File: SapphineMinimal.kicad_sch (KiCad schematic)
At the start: 0 parts

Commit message: daily update
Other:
- note added: "Optional Winc1500 WiFi module add on"
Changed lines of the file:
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@@
+    (stroke (width 0) (type default) (color 0 0 0 0))
+  )
+  (polyline (pts (xy 165.1 123.19) (xy 165.1 168.91))
     (stroke (width 0) (type default) (color 0 0 0 0))
   )
@@
     (stroke (width 0) (type default) (color 0 0 0 0))
   )
+  (polyline (pts (xy 255.27 123.19) (xy 255.27 168.91))
+    (stroke (width 0) (type default) (color 0 0 0 0))
+  )
   (wire (pts (xy 30.48 20.32) (xy 29.21 21.59))
     (stroke (width 0) (type default) (color 0 0 0 0))
@@
     (stroke (width 0) (type default) (color 0 0 0 0))
   )
+  (polyline (pts (xy 255.27 168.91) (xy 165.1 168.91))
+    (stroke (width 0) (type default) (color 0 0 0 0))
+  )
   (wire (pts (xy 162.56 110.49) (xy 203.2 110.49))
     (stroke (width 0) (type default) (color 0 0 0 0))
@@
     (stroke (width 0) (type default) (color 0 0 0 0))
   )
+  (polyline (pts (xy 166.37 123.19) (xy 255.27 123.19))
+    (stroke (width 0) (type default) (color 0 0 0 0))
+  )
   (wire (pts (xy 67.31 68.58) (xy 111.76 68.58))
     (stroke (width 0) (type default) (color 0 0 0 0))
@@
   (wire (pts (xy 48.26 90.17) (xy 111.76 90.17))
     (stroke (width 0) (type default) (color 0 0 0 0))
+  )
+  (text "Optional Winc1500 WiFi module add on" (at 172.72 166.37 0)
+    (effects (font (size 1.27 1.27)) (justify left bottom))
   )
   (label "P3V3" (at 21.59 64.77 0)
@@
       (reference "R306") (unit 1) (value "0") (footprint "Resistor_SMD:R_0603_1608Metric")
     )
+    (path "/00000000-0000-0000-0000-00005e3feed8/daf0bd99-befa-4f90-9212-4e1a6269e40c"
+      (reference "R307") (unit 1) (value "47") (footprint "Resistor_SMD:R_0603_1608Metric")
+    )
+    (path "/00000000-0000-0000-0000-00005e3feed8/73b836e8-41a3-4a83-a239-43a97f5d54a3"
+      (reference "R308") (unit 1) (value "47") (footprint "Resistor_SMD:R_0603_1608Metric")
+    )
+    (path "/00000000-0000-0000-0000-00005e3feed8/15b51247-f7d4-4fb2-a281-1d0f0d3ebd69"
+      (reference "R309") (unit 1) (value "47") (footprint "Resistor_SMD:R_0603_1608Metric")
+    )
+    (path "/00000000-0000-0000-0000-00005e3feed8/8bee83c3-4740-451a-ae50-53d5532ca793"
+      (reference "R310") (unit 1) (value "47") (footprint "Resistor_SMD:R_0603_1608Metric")
+    )
     (path "/00000000-0000-0000-0000-00005e3fe93a/00000000-0000-0000-0000-00005e48c1be"
       (reference "R401") (unit 1) (value "47") (footprint "Resistor_SMD:R_0603_1608Metric")
@@
       (reference "R701") (unit 1) (value "0R25") (footprint "Resistor_SMD:R_0603_1608Metric")
     )
+    (path "/00000000-0000-0000-0000-000063a74ef2/6d43920e-21c5-441e-8415-c5dfb7b75379"
+      (reference "R702") (unit 1) (value "47") (footprint "Resistor_SMD:R_0603_1608Metric")
+    )
+    (path "/00000000-0000-0000-0000-000063a74ef2/44066c90-8c1b-4164-acc8-5fad27e22e40"
+      (reference "R703") (unit 1) (value "47") (footprint "Resistor_SMD:R_0603_1608Metric")
+    )
     (path "/00000000-0000-0000-0000-000063357571/00000000-0000-0000-0000-0000634d9925"
       (reference "R801") (unit 1) (value "4K75") (footprint "Resistor_SMD:R_0603_1608Metric")
@@
       (reference "R838") (unit 1) (value "47K5") (footprint "Resistor_SMD:R_0603_1608Metric")
     )
+    (path "/00000000-0000-0000-0000-000063357571/4b0fc5c4-e883-4a22-b9a8-4f7d5505cc14"
+      (reference "R839") (unit 1) (value "47") (footprint "Resistor_SMD:R_0603_1608Metric")
+    )
+    (path "/00000000-0000-0000-0000-000063357571/0ba43dcf-e8ac-4b48-84ad-6973602d256f"
+      (reference "R840") (unit 1) (value "47") (footprint "Resistor_SMD:R_0603_1608Metric")
+    )
+    (path "/00000000-0000-0000-0000-000063357571/0c45c3ff-9887-4163-9704-1098ef8613b4"
+      (reference "R841") (unit 1) (value "47") (footprint "Resistor_SMD:R_0603_1608Metric")
+    )
+    (path "/00000000-0000-0000-0000-000063357571/ef6922cb-e889-42f1-8d57-45ab4f8f15cc"
+      (reference "R842") (unit 1) (value "47") (footprint "Resistor_SMD:R_0603_1608Metric")
+    )
     (path "/00000000-0000-0000-0000-00005e3fe3dd/00000000-0000-0000-0000-000060b7a41f"

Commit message: Checkpoint
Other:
- sheet SapphireMini_GNSS ports: added GNSS_OUTPUT_POWER; removed GNSS_PWR
- sheet SapphireMini_Power ports: added GNSS_OUTPUT_POWER, GNSS_PWR, SD_OUTPUT_POWER, SD_PWR; removed none
- sheet SapphireMini_SD ports: added SD_OUTPUT_POWER; removed SD_PWR
- sheet Sapphire_Proc ports: added P3V3; removed none
- sheet Sapphire_WiFi ports: added P3V3; removed none

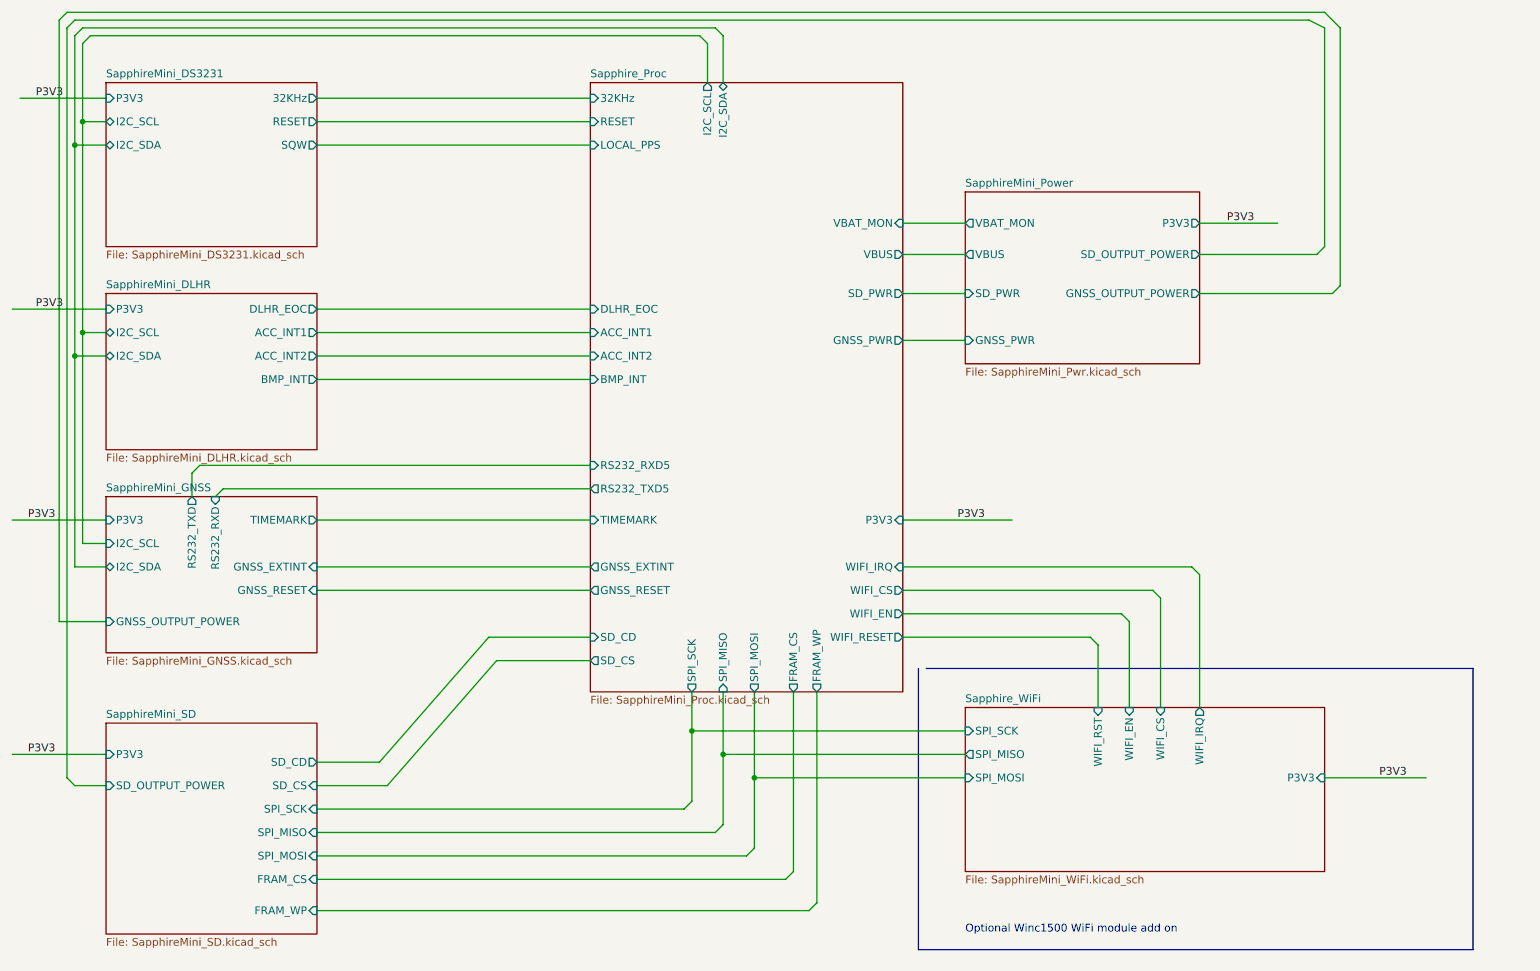
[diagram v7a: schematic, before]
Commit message: Updating for parts avail
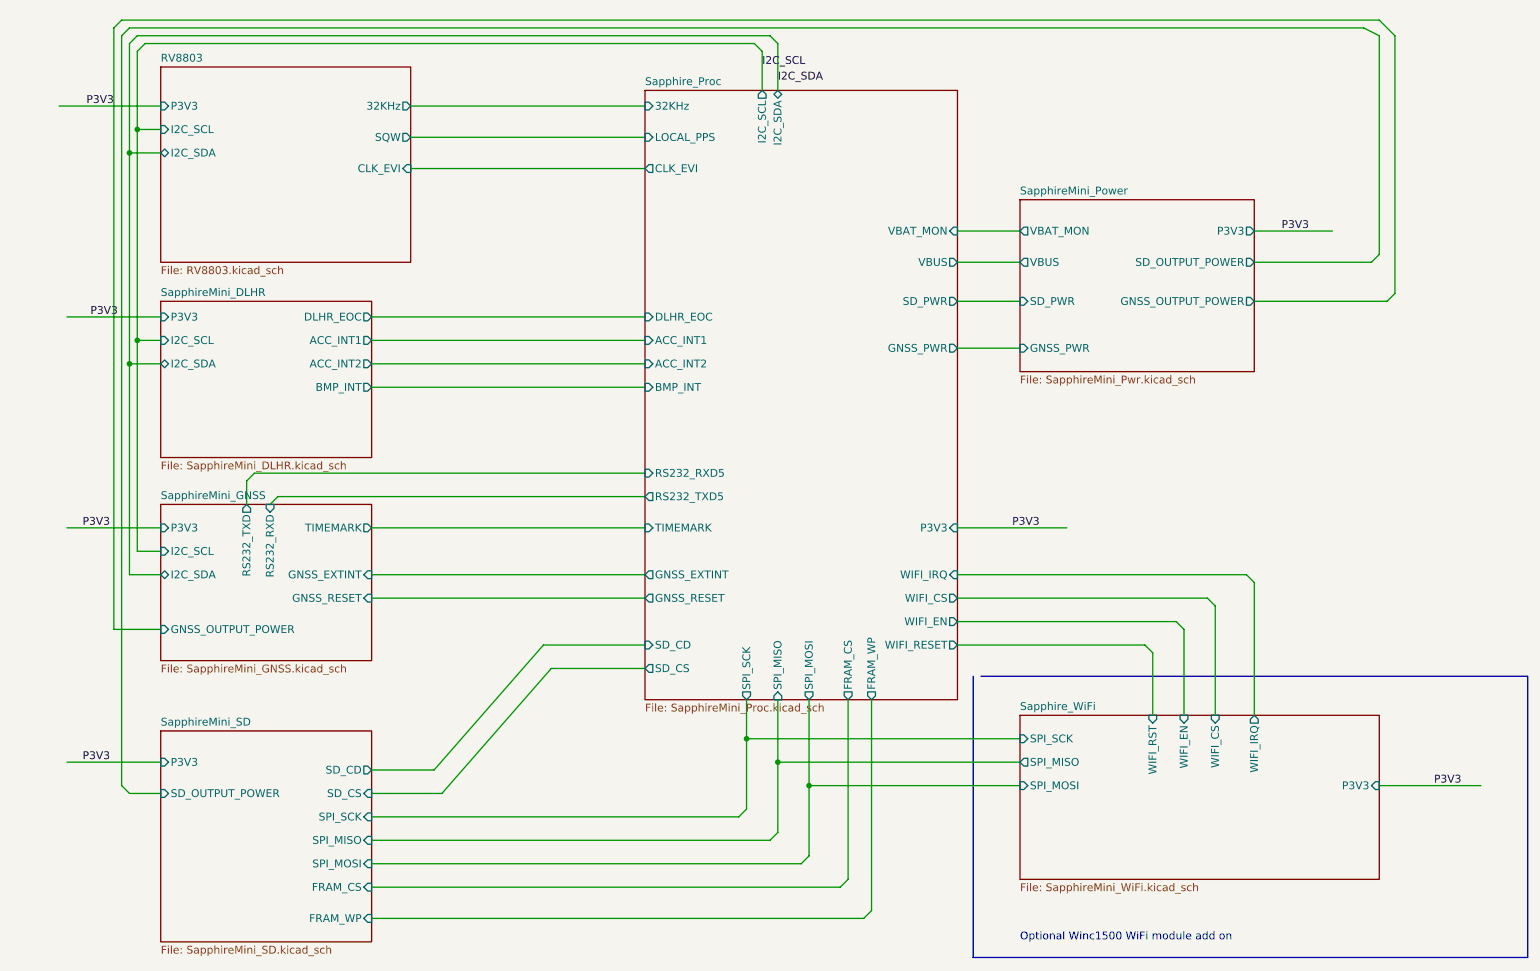
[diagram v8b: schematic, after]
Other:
- removed sheet SapphireMini_DS3231
- added sheet RV8803 (RV8803.kicad_sch)
- sheet Sapphire_Proc ports: added CLK_EVI; removed RESET
